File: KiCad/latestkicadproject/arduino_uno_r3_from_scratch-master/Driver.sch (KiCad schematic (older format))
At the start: 6 parts, among them U1 L298, U3 74AHC1G04, U4 74AHC1G04

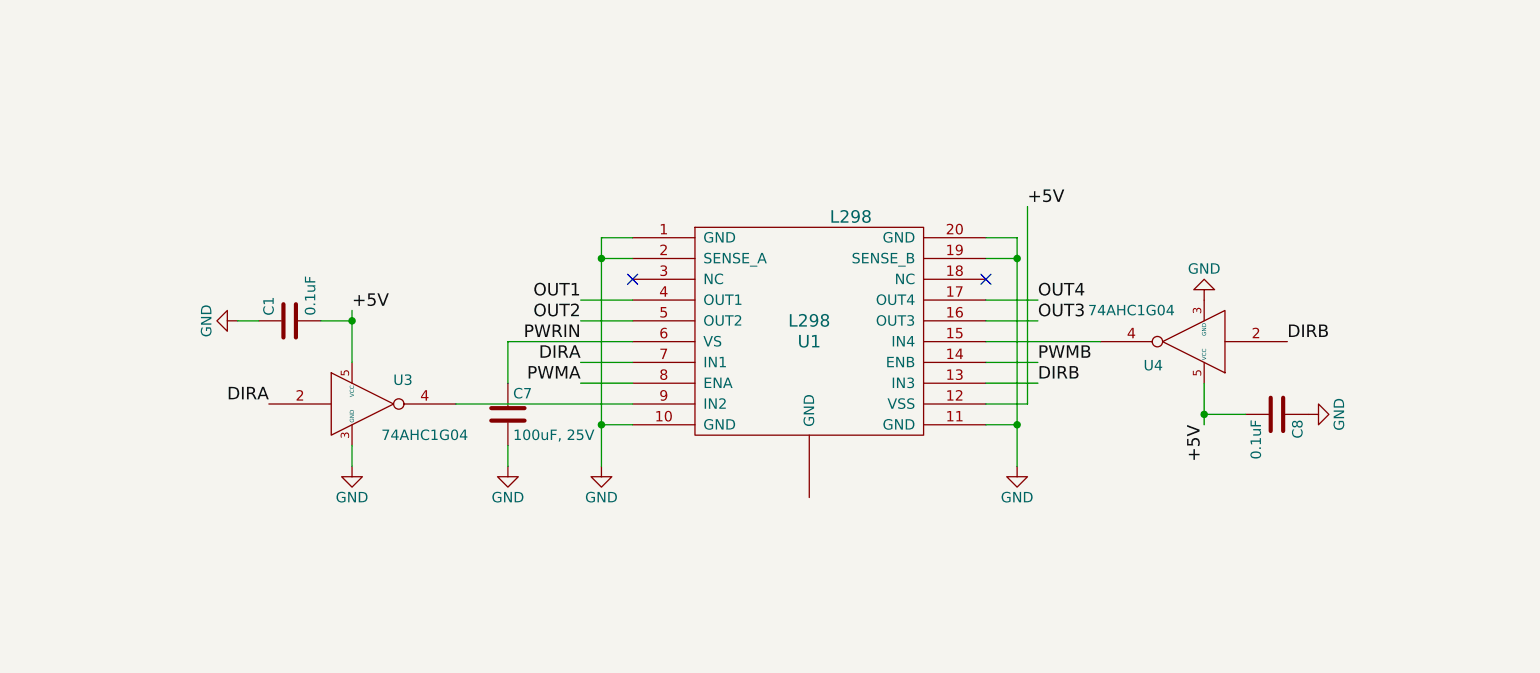
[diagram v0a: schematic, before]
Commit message: 28feb
Aanpassing KiCad+deel footprints
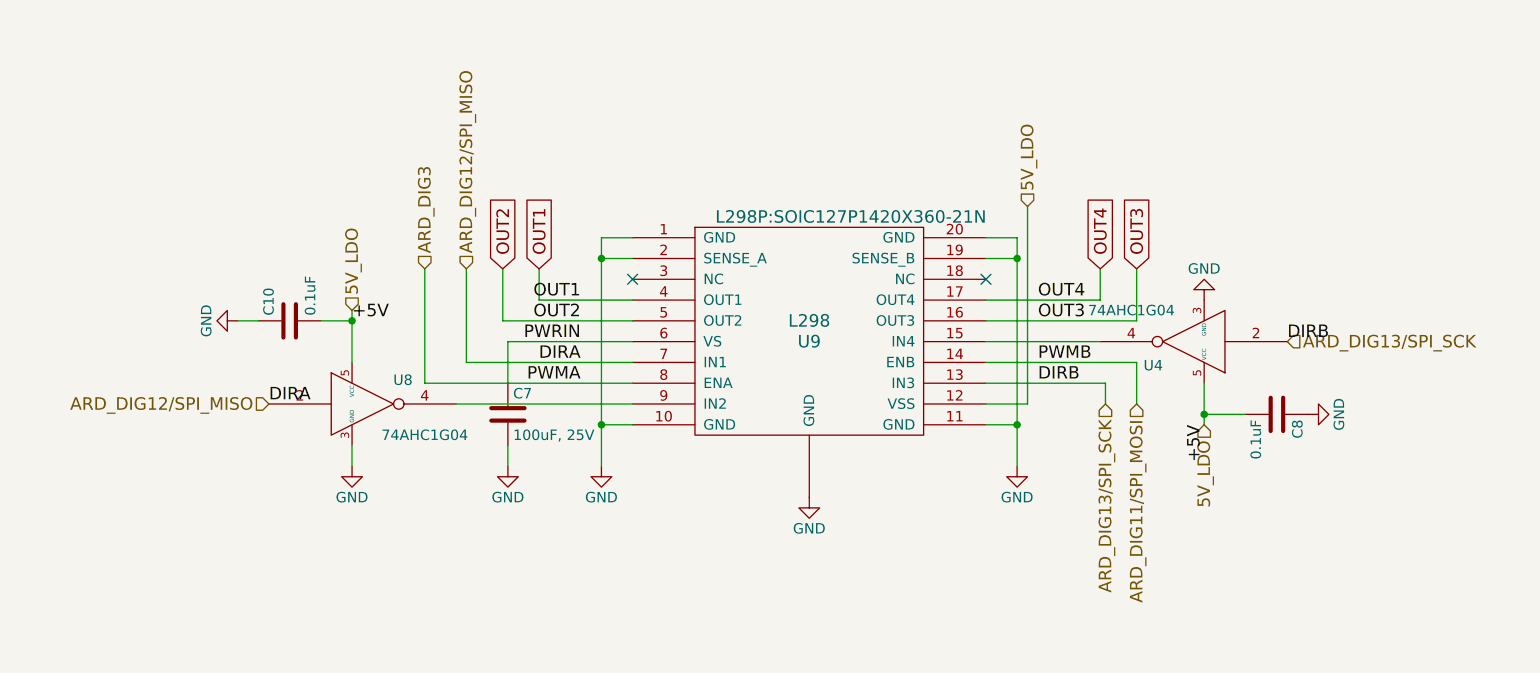
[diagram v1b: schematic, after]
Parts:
- C10: renamed from C1; footprint (none) -> Capacitor_SMD:C_0805_2012Metric
- C7, C8: footprint (none) -> Capacitor_SMD:C_0805_2012Metric
- U9: renamed from U1; footprint L298 -> L298P:SOIC127P1420X360-21N
- renumbered U3 to U8
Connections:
- net GND: now also U9.~ (GND)
- net +5V renamed 5V_LDO
- net DIRA renamed ARD_DIG12/SPI_MISO
- net DIRB renamed ARD_DIG13/SPI_SCK
- net PWMA renamed ARD_DIG3
- net PWMB renamed ARD_DIG11/SPI_MOSI
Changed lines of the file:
@@
 $Descr A4 11693 8268
 encoding utf-8
-Sheet 7 7
+Sheet 6 7
 Title ""
 Date ""
@@
 $EndDescr
 $Comp
-L GND #PWR033
+L GND #PWR025
 U 1 1 5A0B4BA1
 P 4250 3300
-F 0 "#PWR033" H 4250 3050 50  0001 C CNN
+F 0 "#PWR025" H 4250 3050 50  0001 C CNN
 F 1 "GND" H 4250 3150 50  0000 C CNN
 F 2 "" H 4250 3300 50  0001 C CNN
@@
 	4400 2200 4250 2200
 Wire Wire Line
-	4250 2200 4250 3300
-Wire Wire Line
 	4400 2300 4250 2300
 Connection ~ 4250 2300
@@
 Connection ~ 4250 3100
 $Comp
-L GND #PWR034
+L GND #PWR026
 U 1 1 5A0B4C37
 P 6250 3300
-F 0 "#PWR034" H 6250 3050 50  0001 C CNN
+F 0 "#PWR026" H 6250 3050 50  0001 C CNN
 F 1 "GND" H 6250 3150 50  0000 C CNN
 F 2 "" H 6250 3300 50  0001 C CNN
@@
 Connection ~ 6250 3100
 Wire Wire Line
-	6100 2500 6350 2500
-Wire Wire Line
-	6100 2600 6350 2600
+	6100 2500 6650 2500
+Wire Wire Line
+	6100 2600 6825 2600
 Text Label 6350 2500 0    60   ~ 0
 OUT4
@@
 OUT3
 Wire Wire Line
-	6100 2800 6350 2800
-Wire Wire Line
-	6100 2900 6350 2900
+	6100 2800 6825 2800
+Wire Wire Line
+	6100 2900 6675 2900
 Text Label 6350 2800 0    60   ~ 0
 PWMB
@@
 Wire Wire Line
 	6300 3000 6300 2050
-Text Label 6300 2050 0    60   ~ 0
-+5V
 $Comp
 L 74AHC1G04 U4
@@
 	6100 2700 6650 2700
 $Comp
-L GND #PWR035
+L GND #PWR027
 U 1 1 5A0B4D89
 P 7150 2500
-F 0 "#PWR035" H 7150 2250 50  0001 C CNN
+F 0 "#PWR027" H 7150 2250 50  0001 C CNN
 F 1 "GND" H 7150 2350 50  0000 C CNN
 F 2 "" H 7150 2500 50  0001 C CNN
@@
 F 0 "C8" H 7525 3150 50  0000 L CNN
 F 1 "0.1uF" H 7525 2950 50  0000 L CNN
-F 2 "" H 7538 2900 50  0001 C CNN
+F 2 "Capacitor_SMD:C_0805_2012Metric" H 7538 2900 50  0001 C CNN
 F 3 "" H 7500 3050 50  0001 C CNN
 	1    7500 3050
@@
 $EndComp
 $Comp
-L GND #PWR036
+L GND #PWR028
 U 1 1 5A0B5004
 P 7650 3050
-F 0 "#PWR036" H 7650 2800 50  0001 C CNN
+F 0 "#PWR028" H 7650 2800 50  0001 C CNN
 F 1 "GND" H 7650 2900 50  0000 C CNN
 F 2 "" H 7650 3050 50  0001 C CNN
@@
 DIRB
 $Comp
-L L298 U1
+L L298 U9
 U 1 1 5A0B4B28
 P 5250 2700
-F 0 "U1" H 5250 2700 60  0000 C CNN
+F 0 "U9" H 5250 2700 60  0000 C CNN
 F 1 "L298" H 5250 2800 60  0000 C CNN
-F 2 "L298" H 5450 3300 60  0000 C CNN
+F 2 "L298P:SOIC127P1420X360-21N" H 5450 3300 60  0000 C CNN
 F 3 "" H 5250 2700 60  0001 C CNN
 	1    5250 2700
@@
 $EndComp
 Wire Wire Line
-	4400 2500 4150 2500
-Wire Wire Line
-	4400 2600 4150 2600
+	3950 2500 4400 2500
+Wire Wire Line
+	3775 2600 4400 2600
 Wire Wire Line
 	3800 2700 4400 2700
 Wire Wire Line
-	4400 2900 4150 2900
-Wire Wire Line
-	4400 2800 4150 2800
+	3400 2900 4400 2900
+Wire Wire Line
+	3600 2800 4400 2800
 Text Label 4150 2500 2    60   ~ 0
 OUT1
@@
 F 0 "C7" H 3825 3150 50  0000 L CNN
 F 1 "100uF, 25V" H 3825 2950 50  0000 L CNN
-F 2 "" H 3838 2900 50  0001 C CNN
+F 2 "Capacitor_SMD:C_0805_2012Metric" H 3838 2900 50  0001 C CNN
 F 3 "" H 3800 3050 50  0001 C CNN
 	1    3800 3050
@@
 $EndComp
 $Comp
-L GND #PWR037
+L GND #PWR029
 U 1 1 5A0B56EE
 P 3800 3300
-F 0 "#PWR037" H 3800 3050 50  0001 C CNN
+F 0 "#PWR029" H 3800 3050 50  0001 C CNN
 F 1 "GND" H 3800 3150 50  0000 C CNN
 F 2 "" H 3800 3300 50  0001 C CNN
@@
 	3800 3200 3800 3300
 $Comp
-L 74AHC1G04 U3
+L 74AHC1G04 U8
 U 1 1 5A0B58F7
 P 3100 3000
-F 0 "U3" H 3295 3115 50  0000 C CNN
+F 0 "U8" H 3295 3115 50  0000 C CNN
 F 1 "74AHC1G04" H 3400 2850 50  0000 C CNN
 F 2 "" H 3100 3000 50  0001 C CNN
@@
 	4400 3000 3550 3000
 $Comp
-L GND #PWR038
+L GND #PWR030
 U 1 1 5A0B5AAE
 P 3050 3300
-F 0 "#PWR038" H 3050 3050 50  0001 C CNN
+F 0 "#PWR030" H 3050 3050 50  0001 C CNN
 F 1 "GND" H 3050 3150 50  0000 C CNN
 F 2 "" H 3050 3300 50  0001 C CNN
@@
 $EndComp
 Wire Wire Line
-	3050 3300 3050 3200
-Wire Wire Line
 	3050 2550 3050 2800
 Wire Wire Line
 	3050 2600 2900 2600
 Connection ~ 3050 2600
-Text Label 3050 2550 0    60   ~ 0
+Text Label 3050 2600 0    60   ~ 0
 +5V
-Text Label 2650 3000 2    60   ~ 0
+Text Label 2650 3000 0    60   ~ 0
 DIRA
 $Comp
-L C C1
+L C C10
 U 1 1 5A0B5B71
 P 2750 2600
-F 0 "C1" H 2775 2700 50  0000 L CNN
+F 0 "C10" H 2775 2700 50  0000 L CNN
 F 1 "0.1uF" H 2775 2500 50  0000 L CNN
-F 2 "" H 2788 2450 50  0001 C CNN
+F 2 "Capacitor_SMD:C_0805_2012Metric" H 2788 2450 50  0001 C CNN
 F 3 "" H 2750 2600 50  0001 C CNN
 	1    2750 2600
@@
 $EndComp
 $Comp
-L GND #PWR039
+L GND #PWR031
 U 1 1 5A0B5C08
 P 2500 2600
-F 0 "#PWR039" H 2500 2350 50  0001 C CNN
+F 0 "#PWR031" H 2500 2350 50  0001 C CNN
 F 1 "GND" H 2500 2450 50  0000 C CNN
 F 2 "" H 2500 2600 50  0001 C CNN
@@
 NoConn ~ 4400 2400
 NoConn ~ 6100 2400
+Text GLabel 3950 2350 1    60   Input ~ 0
+OUT1
+Text GLabel 3775 2350 1    60   Input ~ 0
+OUT2
+Wire Wire Line
+	3950 2350 3950 2500
+Wire Wire Line
+	3775 2600 3775 2350
+Wire Wire Line
+	3600 2800 3600 2350
+Wire Wire Line
+	3400 2350 3400 2900
+Text GLabel 6650 2350 1    60   Input ~ 0
+OUT4
+Text GLabel 6825 2350 1    60   Input ~ 0
+OUT3
+Wire Wire Line
+	6650 2500 6650 2350
+Wire Wire Line
+	6825 2600 6825 2350
+Wire Wire Line
+	6675 2900 6675 3000
+Wire Wire Line
+	6825 2800 6825 3000
+Wire Wire Line
+	4250 2200 4250 3300
+$Comp
+L GND #PWR032
+U 1 1 5A979197
+P 5250 3450
+F 0 "#PWR032" H 5250 3200 50  0001 C CNN
+F 1 "GND" H 5250 3300 50  0000 C CNN
+F 2 "" H 5250 3450 50  0001 C CNN
+F 3 "" H 5250 3450 50  0001 C CNN
+	1    5250 3450
+	1    0    0    -1
+$EndComp
+Wire Wire Line
+	3050 3300 3050 3200
+Text HLabel 3050 2550 1    60   Input ~ 0
+5V_LDO
+Text HLabel 3400 2350 1    60   Input ~ 0
+ARD_DIG3
+Text HLabel 3600 2350 1    60   Input ~ 0
+ARD_DIG12/SPI_MISO
+Text HLabel 2650 3000 0    60   Input ~ 0
+ARD_DIG12/SPI_MISO
+Text HLabel 6300 2050 1    60   Input ~ 0
+5V_LDO
+Text HLabel 7150 3100 3    60   Input ~ 0
+5V_LDO
+Text HLabel 6675 3000 3    60   Input ~ 0
+ARD_DIG13/SPI_SCK
+Text HLabel 6825 3000 3    60   Input ~ 0
+ARD_DIG11/SPI_MOSI
+Text HLabel 7550 2700 2    60   Input ~ 0
+ARD_DIG13/SPI_SCK
 $EndSCHEMATC

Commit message: Toevoegen footprints Kicad
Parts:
- U4, U8: footprint (none) -> 74AHc1G04:74AHC1G04GW
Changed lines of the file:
@@
 F 0 "U4" H 7295 2815 50  0000 C CNN
 F 1 "74AHC1G04" H 7400 2550 50  0000 C CNN
-F 2 "" H 7100 2700 50  0001 C CNN
+F 2 "74AHc1G04:74AHC1G04GW" H 7100 2700 50  0001 C CNN
 F 3 "" H 7100 2700 50  0001 C CNN
 	1    7100 2700
@@
 F 0 "U8" H 3295 3115 50  0000 C CNN
 F 1 "74AHC1G04" H 3400 2850 50  0000 C CNN
-F 2 "" H 3100 3000 50  0001 C CNN
+F 2 "74AHc1G04:74AHC1G04GW" H 3100 3000 50  0001 C CNN
 F 3 "" H 3100 3000 50  0001 C CNN
 	1    3100 3000

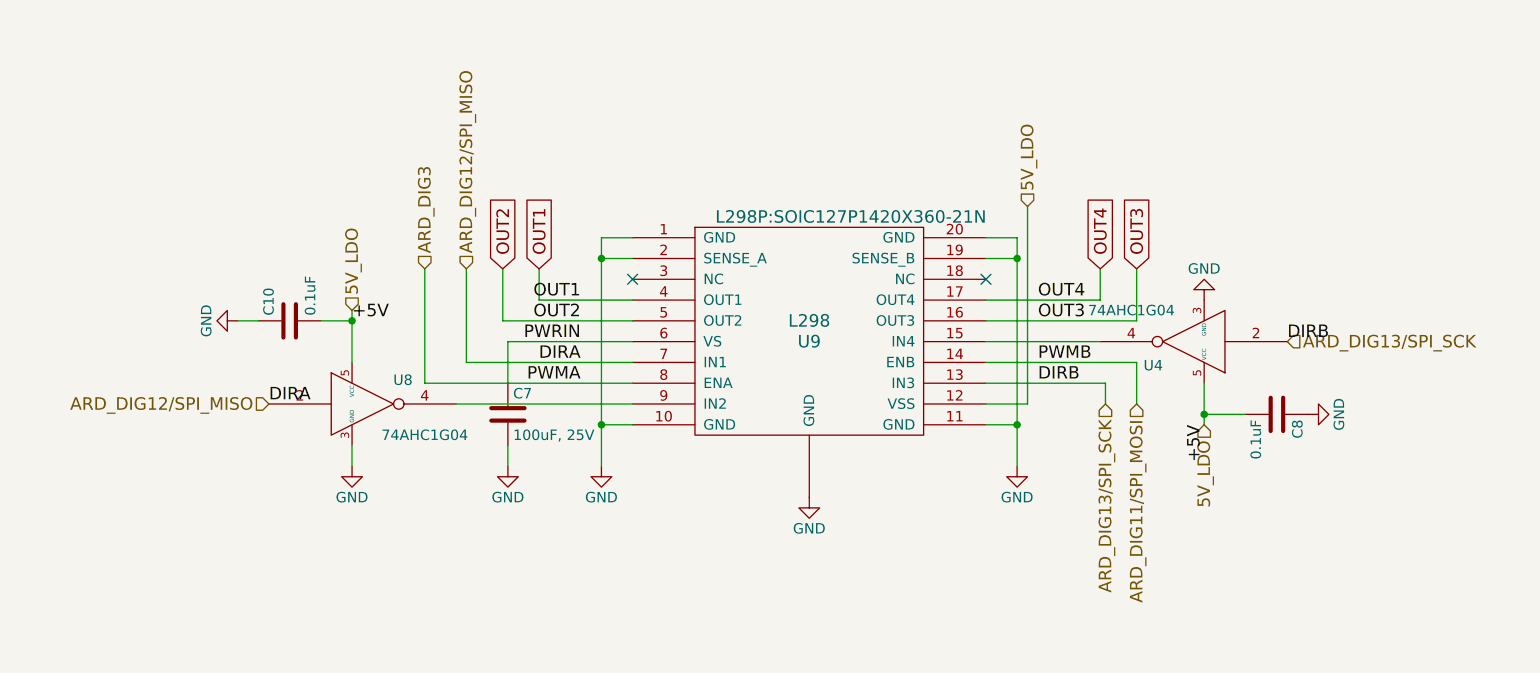
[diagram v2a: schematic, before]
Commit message: Aanpassing KiCad PCB ontwerp + footprints
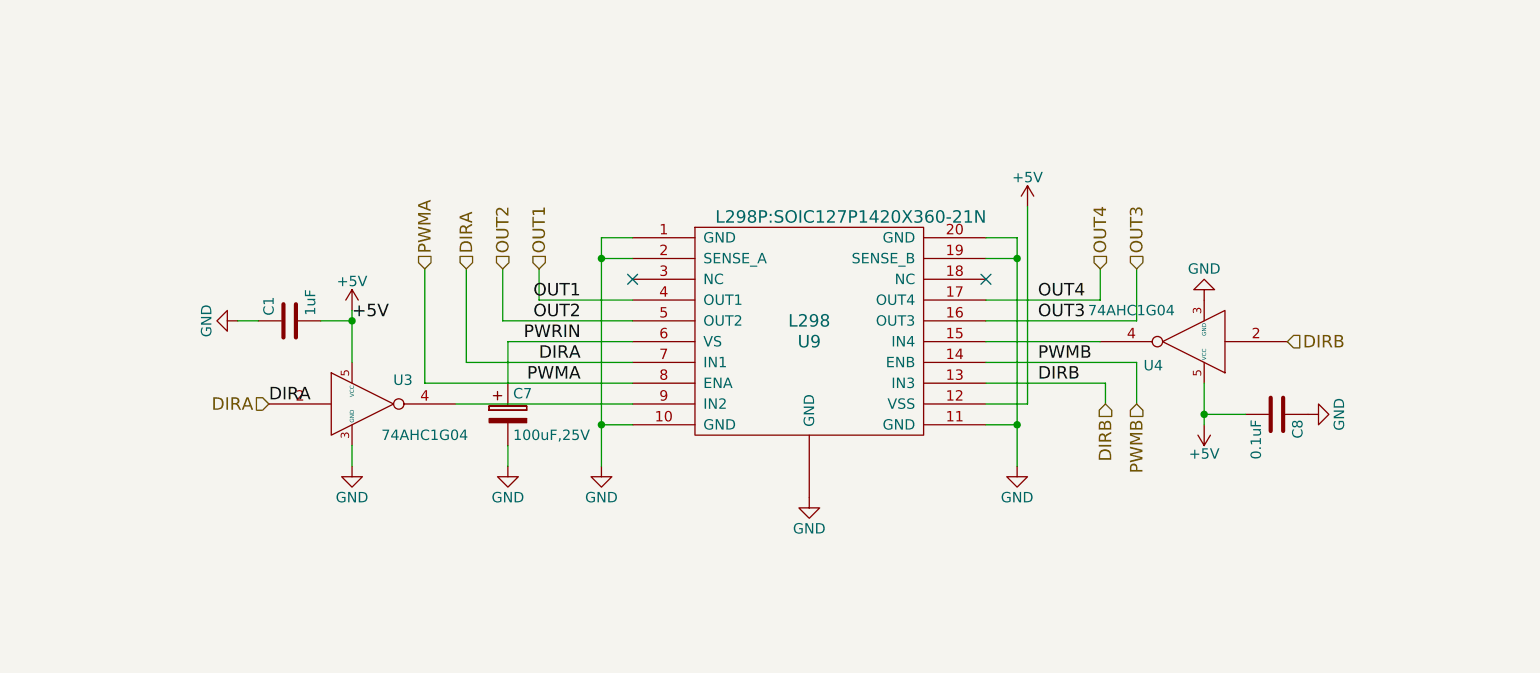
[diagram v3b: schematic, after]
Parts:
- removed C7: 100uF, 25V, Capacitor_SMD:C_0805_2012Metric, symbol C
- added C7: 100uF,25V, Capacitors_SMD:C_0805_HandSoldering, symbol CP
- C1: renamed from C10; value 0.1uF -> 1uF
- renumbered U8 to U3
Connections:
- net GND: now also C7.2
- net PWRIN: now also C7.1
- net 5V_LDO renamed +5V
- net ARD_DIG11/SPI_MOSI renamed PWMB
- net ARD_DIG12/SPI_MISO renamed DIRA
- net ARD_DIG13/SPI_SCK renamed DIRB
- net ARD_DIG3 renamed PWMA
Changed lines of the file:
@@
 LIBS:l298A
 LIBS:Arduino_Uno_R3_From_Scratch-cache
+LIBS:battery
+LIBS:MC33269ST
+LIBS:LP2985-33DBVR
+LIBS:degson
 EELAYER 25 0
 EELAYER END
 $Descr A4 11693 8268
 encoding utf-8
-Sheet 6 7
+Sheet 5 6
 Title ""
 Date ""
@@
 $EndDescr
 $Comp
-L GND #PWR025
+L GND #PWR015
 U 1 1 5A0B4BA1
 P 4250 3300
-F 0 "#PWR025" H 4250 3050 50  0001 C CNN
+F 0 "#PWR015" H 4250 3050 50  0001 C CNN
 F 1 "GND" H 4250 3150 50  0000 C CNN
 F 2 "" H 4250 3300 50  0001 C CNN
@@
 Connection ~ 4250 3100
 $Comp
-L GND #PWR026
+L GND #PWR016
 U 1 1 5A0B4C37
 P 6250 3300
-F 0 "#PWR026" H 6250 3050 50  0001 C CNN
+F 0 "#PWR016" H 6250 3050 50  0001 C CNN
 F 1 "GND" H 6250 3150 50  0000 C CNN
 F 2 "" H 6250 3300 50  0001 C CNN
@@
 	6100 2700 6650 2700
 $Comp
-L GND #PWR027
+L GND #PWR017
 U 1 1 5A0B4D89
 P 7150 2500
-F 0 "#PWR027" H 7150 2250 50  0001 C CNN
+F 0 "#PWR017" H 7150 2250 50  0001 C CNN
 F 1 "GND" H 7150 2350 50  0000 C CNN
 F 2 "" H 7150 2500 50  0001 C CNN
@@
 	7150 3050 7350 3050
 Connection ~ 7150 3050
-Text Label 7150 3100 3    60   ~ 0
-+5V
 $Comp
 L C C8
@@
 $EndComp
 $Comp
-L GND #PWR028
+L GND #PWR018
 U 1 1 5A0B5004
 P 7650 3050
-F 0 "#PWR028" H 7650 2800 50  0001 C CNN
+F 0 "#PWR018" H 7650 2800 50  0001 C CNN
 F 1 "GND" H 7650 2900 50  0000 C CNN
 F 2 "" H 7650 3050 50  0001 C CNN
@@
 	0    -1   -1   0
 $EndComp
-Text Label 7550 2700 0    60   ~ 0
-DIRB
 $Comp
 L L298 U9
@@
 	3800 2700 3800 2900
 $Comp
-L C C7
-U 1 1 5A0B567C
-P 3800 3050
-F 0 "C7" H 3825 3150 50  0000 L CNN
-F 1 "100uF, 25V" H 3825 2950 50  0000 L CNN
-F 2 "Capacitor_SMD:C_0805_2012Metric" H 3838 2900 50  0001 C CNN
-F 3 "" H 3800 3050 50  0001 C CNN
-	1    3800 3050
-	1    0    0    -1
-$EndComp
-$Comp
-L GND #PWR029
+L GND #PWR019
 U 1 1 5A0B56EE
 P 3800 3300
-F 0 "#PWR029" H 3800 3050 50  0001 C CNN
+F 0 "#PWR019" H 3800 3050 50  0001 C CNN
 F 1 "GND" H 3800 3150 50  0000 C CNN
 F 2 "" H 3800 3300 50  0001 C CNN
@@
 	3800 3200 3800 3300
 $Comp
-L 74AHC1G04 U8
+L 74AHC1G04 U3
 U 1 1 5A0B58F7
 P 3100 3000
-F 0 "U8" H 3295 3115 50  0000 C CNN
+F 0 "U3" H 3295 3115 50  0000 C CNN
 F 1 "74AHC1G04" H 3400 2850 50  0000 C CNN
 F 2 "74AHc1G04:74AHC1G04GW" H 3100 3000 50  0001 C CNN
@@
 	4400 3000 3550 3000
 $Comp
-L GND #PWR030
+L GND #PWR020
 U 1 1 5A0B5AAE
 P 3050 3300
-F 0 "#PWR030" H 3050 3050 50  0001 C CNN
+F 0 "#PWR020" H 3050 3050 50  0001 C CNN
 F 1 "GND" H 3050 3150 50  0000 C CNN
 F 2 "" H 3050 3300 50  0001 C CNN
@@
 DIRA
 $Comp
-L C C10
+L C C1
 U 1 1 5A0B5B71
 P 2750 2600
-F 0 "C10" H 2775 2700 50  0000 L CNN
-F 1 "0.1uF" H 2775 2500 50  0000 L CNN
+F 0 "C1" H 2775 2700 50  0000 L CNN
+F 1 "1uF" H 2775 2500 50  0000 L CNN
 F 2 "Capacitor_SMD:C_0805_2012Metric" H 2788 2450 50  0001 C CNN
 F 3 "" H 2750 2600 50  0001 C CNN
@@
 $EndComp
 $Comp
-L GND #PWR031
+L GND #PWR021
 U 1 1 5A0B5C08
 P 2500 2600
-F 0 "#PWR031" H 2500 2350 50  0001 C CNN
+F 0 "#PWR021" H 2500 2350 50  0001 C CNN
 F 1 "GND" H 2500 2450 50  0000 C CNN
 F 2 "" H 2500 2600 50  0001 C CNN
@@
 NoConn ~ 4400 2400
 NoConn ~ 6100 2400
-Text GLabel 3950 2350 1    60   Input ~ 0
-OUT1
-Text GLabel 3775 2350 1    60   Input ~ 0
-OUT2
 Wire Wire Line
 	3950 2350 3950 2500
@@
 Wire Wire Line
 	3400 2350 3400 2900
-Text GLabel 6650 2350 1    60   Input ~ 0
-OUT4
-Text GLabel 6825 2350 1    60   Input ~ 0
-OUT3
 Wire Wire Line
 	6650 2500 6650 2350
@@
 	4250 2200 4250 3300
 $Comp
-L GND #PWR032
+L GND #PWR022
 U 1 1 5A979197
 P 5250 3450
-F 0 "#PWR032" H 5250 3200 50  0001 C CNN
+F 0 "#PWR022" H 5250 3200 50  0001 C CNN
 F 1 "GND" H 5250 3300 50  0000 C CNN
 F 2 "" H 5250 3450 50  0001 C CNN
@@
 Wire Wire Line
 	3050 3300 3050 3200
-Text HLabel 3050 2550 1    60   Input ~ 0
-5V_LDO
 Text HLabel 3400 2350 1    60   Input ~ 0
-ARD_DIG3
+PWMA
 Text HLabel 3600 2350 1    60   Input ~ 0
-ARD_DIG12/SPI_MISO
+DIRA
 Text HLabel 2650 3000 0    60   Input ~ 0
-ARD_DIG12/SPI_MISO
-Text HLabel 6300 2050 1    60   Input ~ 0
-5V_LDO
-Text HLabel 7150 3100 3    60   Input ~ 0
-5V_LDO
+DIRA
 Text HLabel 6675 3000 3    60   Input ~ 0
-ARD_DIG13/SPI_SCK
+DIRB
 Text HLabel 6825 3000 3    60   Input ~ 0
-ARD_DIG11/SPI_MOSI
+PWMB
 Text HLabel 7550 2700 2    60   Input ~ 0
-ARD_DIG13/SPI_SCK
+DIRB
+$Comp
+L +5V #PWR023
+U 1 1 5AA17AD4
+P 3050 2550
+F 0 "#PWR023" H 3050 2400 50  0001 C CNN
+F 1 "+5V" H 3050 2690 50  0000 C CNN
+F 2 "" H 3050 2550 50  0001 C CNN
+F 3 "" H 3050 2550 50  0001 C CNN
+	1    3050 2550
+	1    0    0    -1
+$EndComp
+$Comp
+L CP C7
+U 1 1 5AA17B72
+P 3800 3050
+F 0 "C7" H 3825 3150 50  0000 L CNN
+F 1 "100uF,25V" H 3825 2950 50  0000 L CNN
+F 2 "Capacitors_SMD:C_0805_HandSoldering" H 3838 2900 50  0001 C CNN
+F 3 "" H 3800 3050 50  0001 C CNN
+	1    3800 3050
+	1    0    0    -1
+$EndComp
+$Comp
+L +5V #PWR024
+U 1 1 5AA17E98
+P 6300 2050
+F 0 "#PWR024" H 6300 1900 50  0001 C CNN
+F 1 "+5V" H 6300 2190 50  0000 C CNN
+F 2 "" H 6300 2050 50  0001 C CNN
+F 3 "" H 6300 2050 50  0001 C CNN
+	1    6300 2050
+	1    0    0    -1
+$EndComp
+$Comp
+L +5V #PWR025
+U 1 1 5AA17EEA
+P 7150 3100
+F 0 "#PWR025" H 7150 2950 50  0001 C CNN
+F 1 "+5V" H 7150 3240 50  0000 C CNN
+F 2 "" H 7150 3100 50  0001 C CNN
+F 3 "" H 7150 3100 50  0001 C CNN
+	1    7150 3100
+	-1   0    0    1
+$EndComp
+Text HLabel 3775 2350 1    60   Input ~ 0
+OUT2
+Text HLabel 3950 2350 1    60   Input ~ 0
+OUT1
+Text HLabel 6650 2350 1    60   Input ~ 0
+OUT4
+Text HLabel 6825 2350 1    60   Input ~ 0
+OUT3
 $EndSCHEMATC
